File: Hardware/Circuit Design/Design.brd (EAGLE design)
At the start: 88.8 x 34.4 mm, 73 parts, among them J1 5362, Q2 FS8205A, U1 HTU21D, U2 TP4056, U3 ATMEGA328P-AU, U4 MT3608, U5 DW01A, Y1 HC-49US

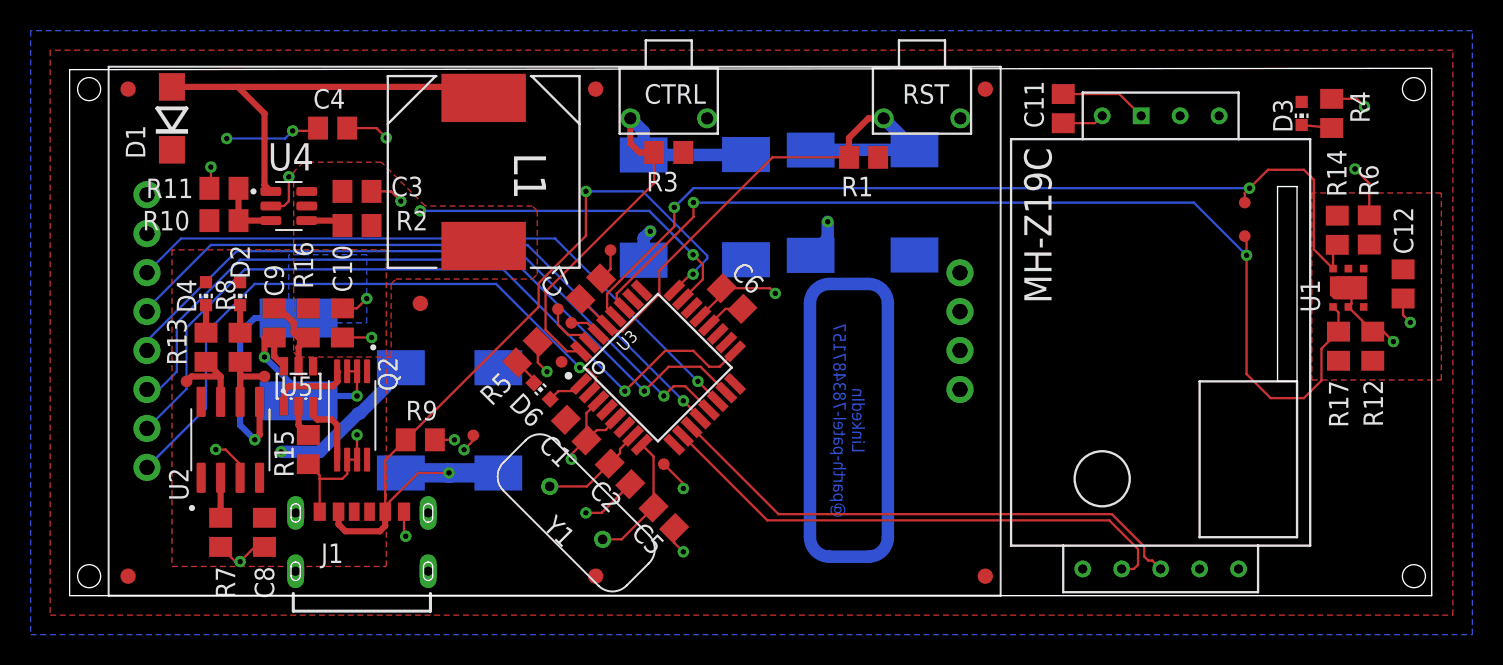
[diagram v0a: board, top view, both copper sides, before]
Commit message: Change Mounting Holes size from M1.5 to M4
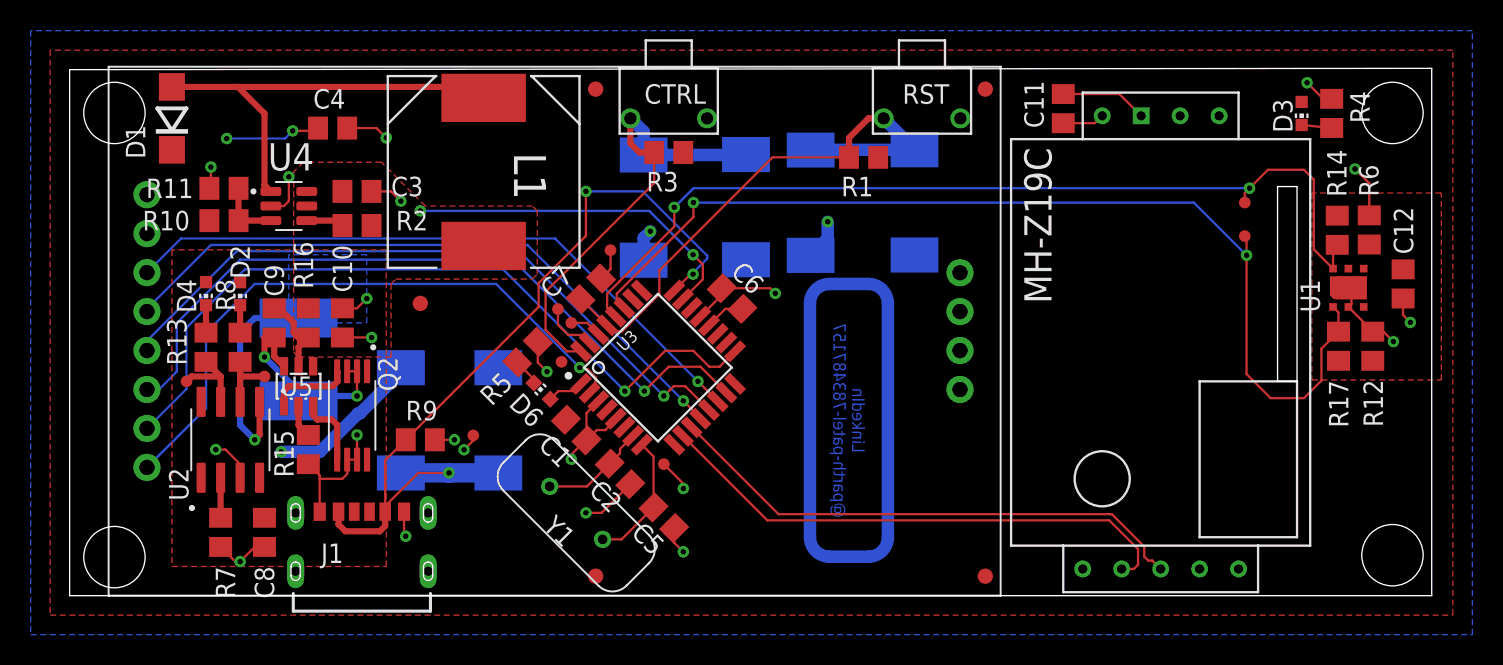
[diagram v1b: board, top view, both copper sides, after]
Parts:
- removed FID6, FID7: FIDUCIAL"", Airquality_Sensor:FIDUCIAL_1MM
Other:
- outline, holes or cut-outs redrawn
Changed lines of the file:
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@@
 <setting verticaltext="up"/>
 </settings>
-<grid distance="0.3125" unitdist="mm" unit="mm" style="lines" multiple="1" display="yes" altdistance="5" altunitdist="mil" altunit="mil"/>
+<grid distance="0.127" unitdist="mm" unit="mm" style="lines" multiple="1" display="yes" altdistance="5" altunitdist="mil" altunit="mm"/>
 <layers>
 <layer number="1" name="Top" color="4" fill="1" visible="yes" active="yes"/>
@@
 <text x="34.925" y="32.0675" size="1.27" layer="25">CTRL</text>
 <text x="51.7525" y="32.0675" size="1.27" layer="25">RST</text>
-<polygon width="0.1524" layer="41">
-<vertex x="83.82" y="34.29"/>
-<vertex x="83.82" y="31.75"/>
-<vertex x="86.36" y="31.75"/>
-<vertex x="86.36" y="34.29"/>
-</polygon>
-<polygon width="0.1524" layer="42">
-<vertex x="83.82" y="34.29"/>
-<vertex x="83.82" y="31.75"/>
-<vertex x="86.36" y="31.75"/>
-<vertex x="86.36" y="34.29"/>
-</polygon>
-<circle x="85.09" y="33.02" radius="0.75" width="0" layer="20"/>
-<polygon width="0.1524" layer="41">
-<vertex x="83.82" y="2.54"/>
-<vertex x="83.82" y="0"/>
-<vertex x="86.25" y="0"/>
-<vertex x="86.25" y="2.54"/>
-</polygon>
-<polygon width="0.1524" layer="42">
-<vertex x="83.82" y="2.54"/>
-<vertex x="83.82" y="0"/>
-<vertex x="86.25" y="0"/>
-<vertex x="86.25" y="2.54"/>
-</polygon>
-<circle x="85.09" y="1.27" radius="0.75" width="0" layer="20"/>
-<polygon width="0.1524" layer="41">
-<vertex x="-2.54" y="2.54"/>
-<vertex x="-2.54" y="0"/>
-<vertex x="0" y="0"/>
-<vertex x="0" y="2.54"/>
-</polygon>
-<polygon width="0.1524" layer="42">
-<vertex x="-2.54" y="2.54"/>
-<vertex x="-2.54" y="0"/>
-<vertex x="0" y="0"/>
-<vertex x="0" y="2.54"/>
-</polygon>
-<circle x="-1.27" y="1.27" radius="0.75" width="0" layer="20"/>
-<polygon width="0.1524" layer="41">
-<vertex x="-2.54" y="34.29"/>
-<vertex x="-2.54" y="31.75"/>
-<vertex x="0" y="31.75"/>
-<vertex x="0" y="34.29"/>
-</polygon>
-<polygon width="0.1524" layer="42">
-<vertex x="-2.54" y="34.29"/>
-<vertex x="-2.54" y="31.75"/>
-<vertex x="0" y="31.75"/>
-<vertex x="0" y="34.29"/>
-</polygon>
-<circle x="-1.27" y="33.02" radius="0.75" width="0" layer="20"/>
 <wire x1="77.47" y1="26.67" x2="77.47" y2="13.97" width="0" layer="20"/>
 <wire x1="77.47" y1="13.97" x2="76.2" y2="13.97" width="0" layer="20"/>
 <wire x1="76.2" y1="13.97" x2="76.2" y2="26.67" width="0" layer="20"/>
 <wire x1="76.2" y1="26.67" x2="77.47" y2="26.67" width="0" layer="20"/>
+<polygon width="0.1524" layer="41">
+<vertex x="80.859" y="34.3005"/>
+<vertex x="80.859" y="28.948"/>
+<vertex x="86.2115" y="28.948"/>
+<vertex x="86.2115" y="34.3005"/>
+</polygon>
+<polygon width="0.1524" layer="42">
+<vertex x="80.859" y="34.3005"/>
+<vertex x="80.859" y="28.948"/>
+<vertex x="86.2115" y="28.948"/>
+<vertex x="86.2115" y="34.3005"/>
+</polygon>
+<circle x="83.6915" y="31.468" radius="2" width="0" layer="20"/>
+<polygon width="0.1524" layer="41">
+<vertex x="-2.453" y="34.3005"/>
+<vertex x="-2.453" y="28.948"/>
+<vertex x="2.8995" y="28.948"/>
+<vertex x="2.8995" y="34.3005"/>
+</polygon>
+<polygon width="0.1524" layer="42">
+<vertex x="-2.453" y="34.3005"/>
+<vertex x="-2.453" y="28.948"/>
+<vertex x="2.8995" y="28.948"/>
+<vertex x="2.8995" y="34.3005"/>
+</polygon>
+<circle x="0.3795" y="31.468" radius="2" width="0" layer="20"/>
+<polygon width="0.1524" layer="41">
+<vertex x="-2.453" y="5.3445"/>
+<vertex x="-2.453" y="-0.008"/>
+<vertex x="2.8995" y="-0.008"/>
+<vertex x="2.8995" y="5.3445"/>
+</polygon>
+<polygon width="0.1524" layer="42">
+<vertex x="-2.453" y="5.3445"/>
+<vertex x="-2.453" y="-0.008"/>
+<vertex x="2.8995" y="-0.008"/>
+<vertex x="2.8995" y="5.3445"/>
+</polygon>
+<circle x="0.3795" y="2.512" radius="2" width="0" layer="20"/>
+<polygon width="0.1524" layer="41">
+<vertex x="80.859" y="5.4715"/>
+<vertex x="80.859" y="0.119"/>
+<vertex x="86.2115" y="0.119"/>
+<vertex x="86.2115" y="5.4715"/>
+</polygon>
+<polygon width="0.1524" layer="42">
+<vertex x="80.859" y="5.4715"/>
+<vertex x="80.859" y="0.119"/>
+<vertex x="86.2115" y="0.119"/>
+<vertex x="86.2115" y="5.4715"/>
+</polygon>
+<circle x="83.6915" y="2.639" radius="2" width="0" layer="20"/>
 </plain>
 <attributes>
@@
 <attribute name="BOM" value="EXCLUDE" x="20.32" y="19.05" size="1.778" layer="27" display="off"/>
 </element>
-<element name="FID6" library="Airquality_Sensor" library_urn="urn:adsk.eagle:library:16015176" package="FIDUCIAL_1MM" package3d_urn="urn:adsk.eagle:package:15955190/2" value="FIDUCIAL&quot;&quot;" x="1.27" y="33.02" smashed="yes">
-<attribute name="BOM" value="EXCLUDE" x="1.27" y="33.02" size="1.778" layer="27" display="off"/>
-</element>
-<element name="FID7" library="Airquality_Sensor" library_urn="urn:adsk.eagle:library:16015176" package="FIDUCIAL_1MM" package3d_urn="urn:adsk.eagle:package:15955190/2" value="FIDUCIAL&quot;&quot;" x="1.27" y="1.27" smashed="yes">
-<attribute name="BOM" value="EXCLUDE" x="1.27" y="1.27" size="1.778" layer="27" display="off"/>
-</element>
 <element name="TP1" library="SparkFun-Connectors" library_urn="urn:adsk.eagle:library:513" package="PAD.03X.03" package3d_urn="urn:adsk.eagle:package:38286/1" value="TEST-POINT3" x="32.7175" y="22.5225" smashed="yes"/>
 <element name="TP2" library="SparkFun-Connectors" library_urn="urn:adsk.eagle:library:513" package="PAD.03X.03" package3d_urn="urn:adsk.eagle:package:38286/1" value="TEST-POINT3" x="30.1625" y="17.78" smashed="yes"/>
@@
 <via x="83.75" y="16.5625" extent="1-16" drill="0.35"/>
 <wire x1="84.3825" y1="19.3725" x2="84.375" y2="19.365" width="0.1524" layer="1"/>
-<wire x1="79.7275" y1="32.3875" x2="81.3625" y2="32.3875" width="0.1524" layer="1"/>
-<wire x1="81.3625" y1="32.3875" x2="81.875" y2="31.875" width="0.1524" layer="1"/>
-<via x="81.875" y="31.875" extent="1-16" drill="0.35"/>
+<wire x1="79.7275" y1="32.3875" x2="79.175" y2="32.3875" width="0.1524" layer="1"/>
+<wire x1="79.175" y1="32.3875" x2="78.125" y2="33.4375" width="0.1524" layer="1"/>
+<via x="78.125" y="33.4375" extent="1-16" drill="0.35"/>
 <wire x1="81.0175" y1="20.07" x2="81.0175" y2="19.02" width="0.1524" layer="1"/>
 <wire x1="81.0175" y1="19.02" x2="80.8175" y2="18.82" width="0.1524" layer="1"/>
